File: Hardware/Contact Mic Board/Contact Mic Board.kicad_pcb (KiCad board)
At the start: 2 copper layers, 38 parts, among them J1 Conn_01x09_Pin, U1 ES8388, U2 MCP6002-xMC

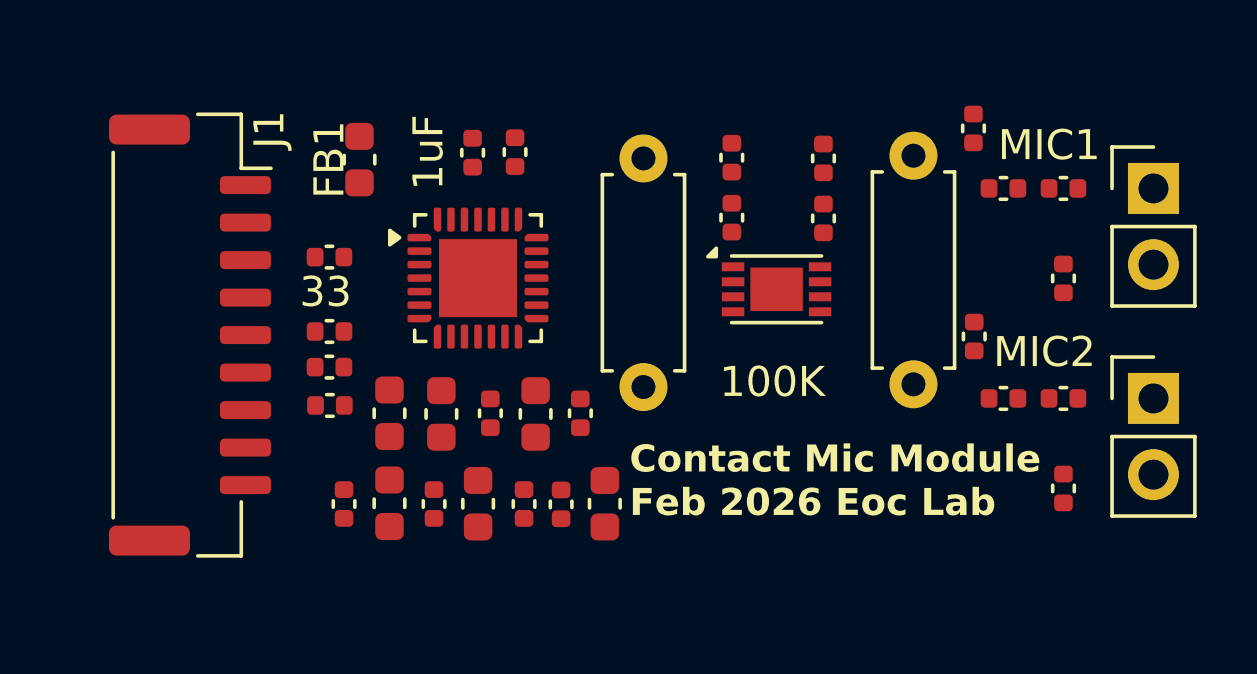
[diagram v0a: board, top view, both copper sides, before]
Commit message: Finalized layout for contact mic board
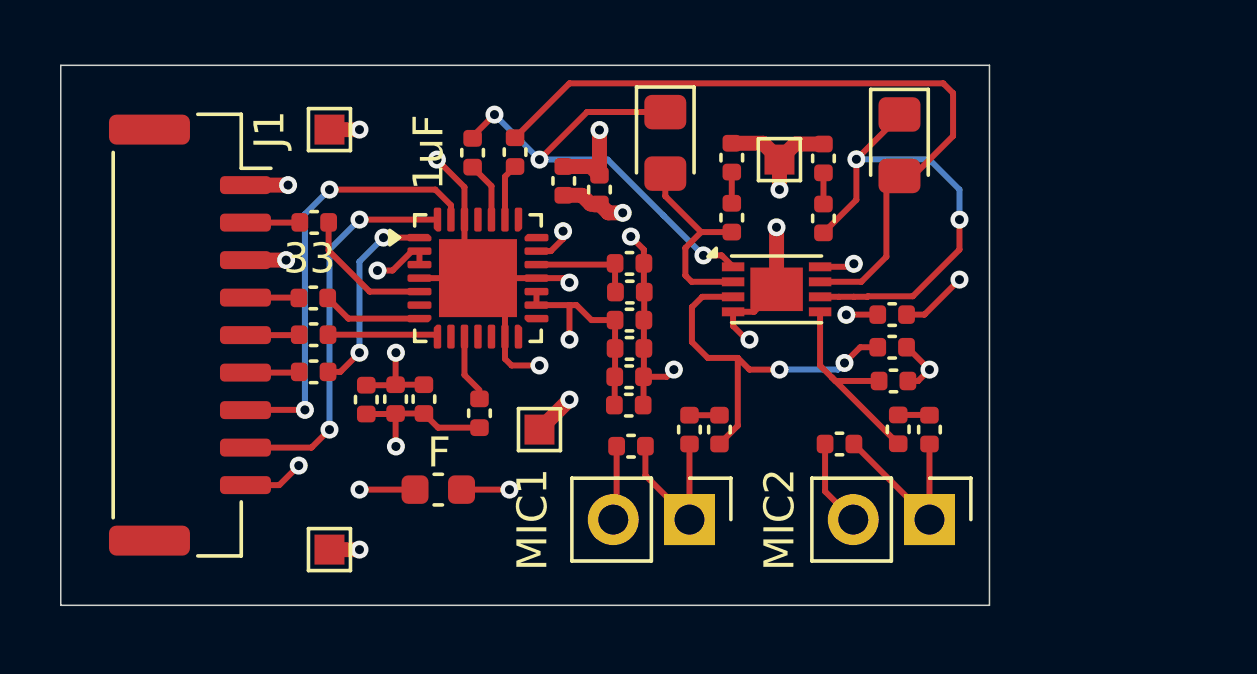
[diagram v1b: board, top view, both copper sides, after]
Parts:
- added C19: 0.1uF, Capacitor_SMD:C_0402_1005Metric, F.Cu at (130.8, 56.2)
- added TP1: TestPoint, TestPoint:TestPoint_Pad_1.0x1.0mm, F.Cu at (112.0, 50.0)
- added TP2: TestPoint, TestPoint:TestPoint_Pad_1.0x1.0mm, F.Cu at (112.0, 64.0)
- added TP3: TestPoint, TestPoint:TestPoint_Pad_1.0x1.0mm, F.Cu at (119.0, 60.0)
- added TP4: TestPoint, TestPoint:TestPoint_Pad_1.0x1.0mm, F.Cu at (127.0, 51.0)
- C14, C15, C17, C2, C4, C7: footprint Capacitor_SMD:C_0603_1608Metric -> Capacitor_SMD:C_0402_1005Metric
- R5, R6: footprint Resistor_THT:R_Axial_DIN0207_L6.3mm_D2.5mm_P7.62mm_Horizontal -> Diode_SMD:D_0805_2012Metric_Pad1.15x1.40mm_HandSolder
- moved MIC1 19.0 mm to (124.0, 63.0), turned to -90 degrees
- moved R9 15.5 mm to (122.1, 60.6), turned to 180 degrees
- moved C8 14.8 mm to (124.0, 60.0), turned to -90 degrees
- moved R1 12.4 mm to (125.0, 60.0), turned to 90 degrees
- moved FB1 11.3 mm to (115.6, 62.0), turned to 180 degrees
- moved MIC2 8.49 mm to (132.0, 63.0), turned to -90 degrees
- moved C15 8.03 mm to (122.0, 54.5), turned to 0 degrees
- moved R5 7.98 mm to (131.0, 50.5), turned to -90 degrees
- moved R3 7.78 mm to (130.8, 57.3), turned to 0 degrees
- moved C17 7.78 mm to (121.0, 52.0), turned to 90 degrees
- moved C18 7.77 mm to (119.8, 51.7), turned to 90 degrees
- moved R10 7.61 mm to (129.0, 60.5), turned to 180 degrees
- moved C4 7.23 mm to (122.0, 57.3), turned to 0 degrees
- moved C5 7.07 mm to (122.0, 56.3), turned to 180 degrees
- moved C16 6.16 mm to (122.0, 55.4), turned to 0 degrees
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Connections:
- net Net-(J1-Pin_9) renamed +3.3V
- net Net-(U1-AVDD) renamed +3.3VA
- net Net-(U1-VMID) renamed VMID
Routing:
- net GND: track 0.00 -> 45.2 mm, vias 0 -> 13
- net Net-(C9-Pad2): track 0.00 -> 24.1 mm
- net Net-(C10-Pad2): track 0.00 -> 16.0 mm, vias 0 -> 3
- net Net-(U2B--): track 0.00 -> 15.5 mm, vias 0 -> 2
- net Net-(J1-Pin_7): track 0.00 -> 14.4 mm, vias 0 -> 2
- net Net-(J1-Pin_8): track 0.00 -> 13.1 mm, vias 0 -> 2
- net Net-(U2A-+): track 0.00 -> 12.7 mm, vias 0 -> 2
- net +3.3VA: track 0.00 -> 12.5 mm, vias 0 -> 5
- net +3.3V: track 0.00 -> 10.0 mm, vias 0 -> 5
- net VMID: track 0.00 -> 10.0 mm, vias 0 -> 4
- net Net-(U2B-+): track 0.00 -> 7.10 mm
- net Net-(U2A--): track 0.00 -> 6.81 mm
- net Net-(U1-MCLK): track 0.00 -> 6.68 mm, vias 0 -> 2
- net Net-(MIC2-+): track 0.00 -> 6.08 mm
- net Net-(MIC1-+): track 0.00 -> 5.57 mm
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- added copper zone on In2.Cu, net +3.3V
- added copper zone on In2.Cu, net +3.3VA
- added copper zone on In1.Cu, net GND
- added copper zone on In2.Cu, net VMID
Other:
- board outline added: 31 x 18 mm
- copper layers 2 -> 4
- board text added: "Contact Mic Module EoC Lab Feb 2026"
- board text added: "F"
- board text removed: "100K"
- board text removed: "Contact Mic Module Feb 2026 Eoc Lab"

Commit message: separated the microphone onto its own schematic as we won't be designing it. Updated the contact mic board
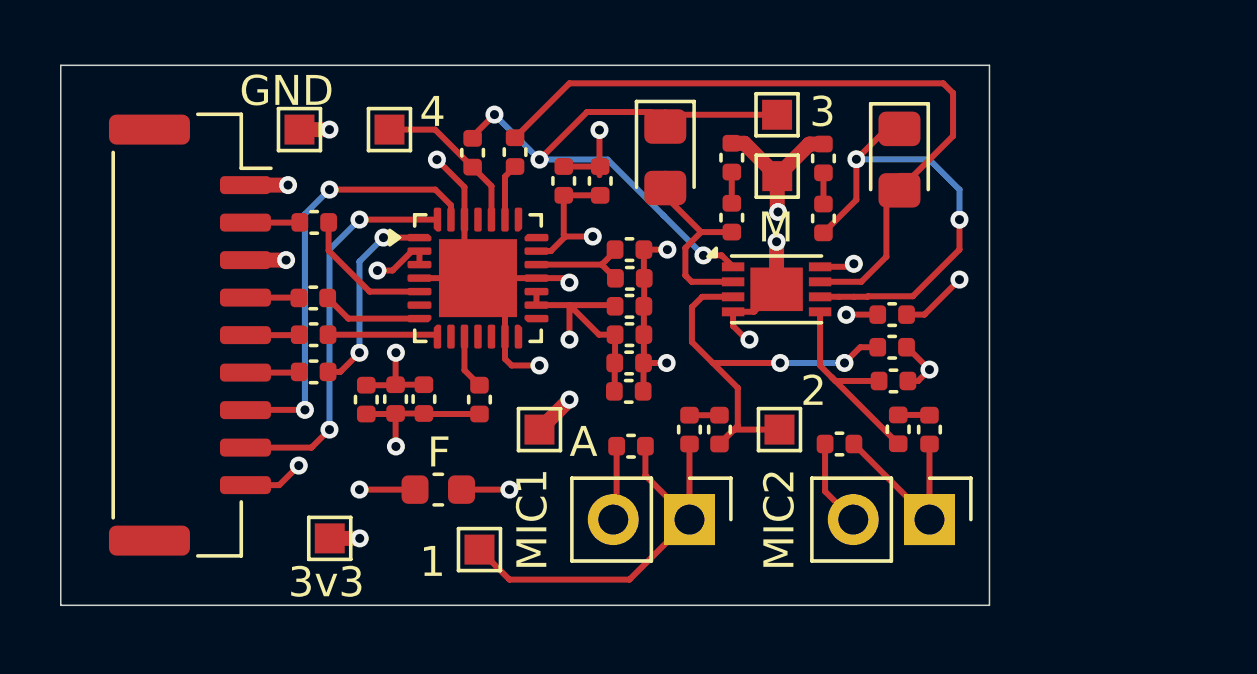
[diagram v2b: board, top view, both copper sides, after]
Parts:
- added TP5: TestPoint, TestPoint:TestPoint_Pad_1.0x1.0mm, F.Cu at (127.0, 60.0)
- added TP6: TestPoint, TestPoint:TestPoint_Pad_1.0x1.0mm, F.Cu at (126.9, 49.5)
- added TP7: TestPoint, TestPoint:TestPoint_Pad_1.0x1.0mm, F.Cu at (114.0, 50.0)
- added TP8: TestPoint, TestPoint:TestPoint_Pad_1.0x1.0mm, F.Cu at (117.0, 64.0)
- moved TP1 1.00 mm to (111.0, 50.0)
- moved TP4 0.56 mm to (126.9, 51.6)
- moved R5 0.48 mm to (131.0, 51.0)
- moved R6 0.48 mm to (123.2, 50.9)
- moved C15 0.46 mm to (122.0, 54.0)
- moved C7 0.46 mm to (122.0, 57.8)
- moved C16 0.46 mm to (122.0, 55.0)
- moved C4 0.46 mm to (122.0, 56.8)
- moved C5 0.46 mm to (122.0, 55.9)
- moved C6 0.46 mm to (122.0, 58.7)
- moved C14 0.46 mm to (117.0, 59.0)
- moved TP2 0.37 mm to (112.0, 63.6)
- moved C17 0.29 mm to (121.0, 51.7)
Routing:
- net Net-(MIC1-+): track 5.57 -> 13.8 mm
- net Net-(C10-Pad2): track 16.0 -> 20.2 mm
- net Net-(U1-LIN1): track 2.01 -> 5.30 mm
- net Net-(U2A-+): track 12.7 -> 14.9 mm
- net VMID: track 10.0 -> 11.8 mm, vias 4 -> 3
- net GND: track 45.2 -> 43.8 mm
- net +3.3VA: track 12.5 -> 13.3 mm
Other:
- board text added: "1"
- board text added: "2"
- board text added: "3"
- board text added: "3v3"
- board text added: "4"
- board text added: "A"
- board text added: "Contact Mic Module EoC Lab Feb 2026 Version 1.0"
- board text added: "GND"
- board text added: "M"
- board text removed: "1uF"
- board text removed: "33"
- board text removed: "Contact Mic Module EoC Lab Feb 2026"
